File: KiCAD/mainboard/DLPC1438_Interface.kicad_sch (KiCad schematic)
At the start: 84 parts, among them IC3 SN74AUP1G06DCKR, IC4 SN74AUP1G06DCKR, IC5 SN74AUP1G06DCKR, IC6 SN74AUP1G06DCKR, IC7 SN74AUP1G06DCKR, IC8 SN74AUP1G06DCKR, J2 Conn_01x07_Pin, J3 Conn_02x05_Odd_Even, J31 Conn_01x08_Pin, J4 Conn_01x05_Pin, J7 Conn_01x05_Pin, U1 TXS0102DCU, U12 ECS-2520MV-xxx-xx, U13 MX25L3233FM2, U14 SN74AUP1G06DCKR, U22 TXS0102DCU, U5 SN74AUP1G06DCKR

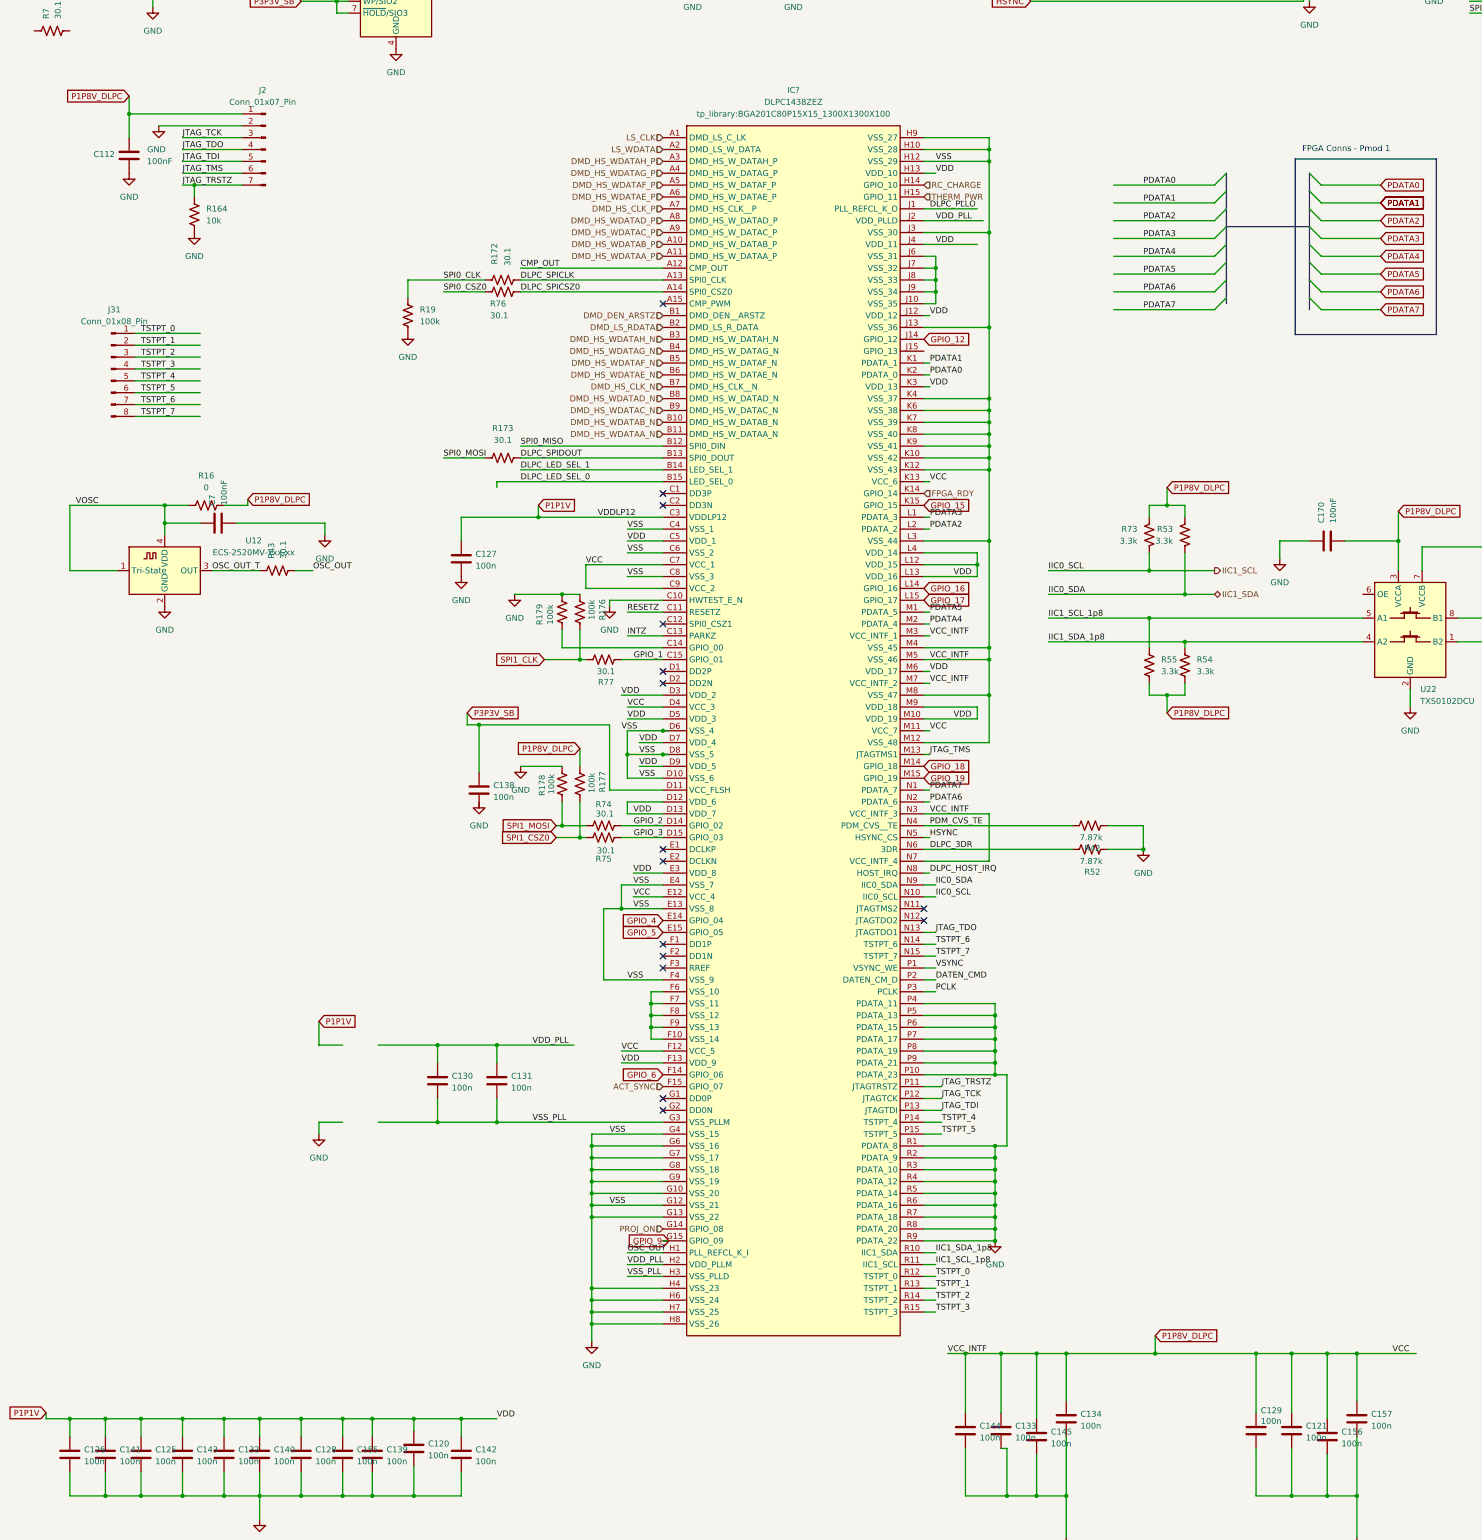
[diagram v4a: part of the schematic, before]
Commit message: fixed bus connection on fpga connector
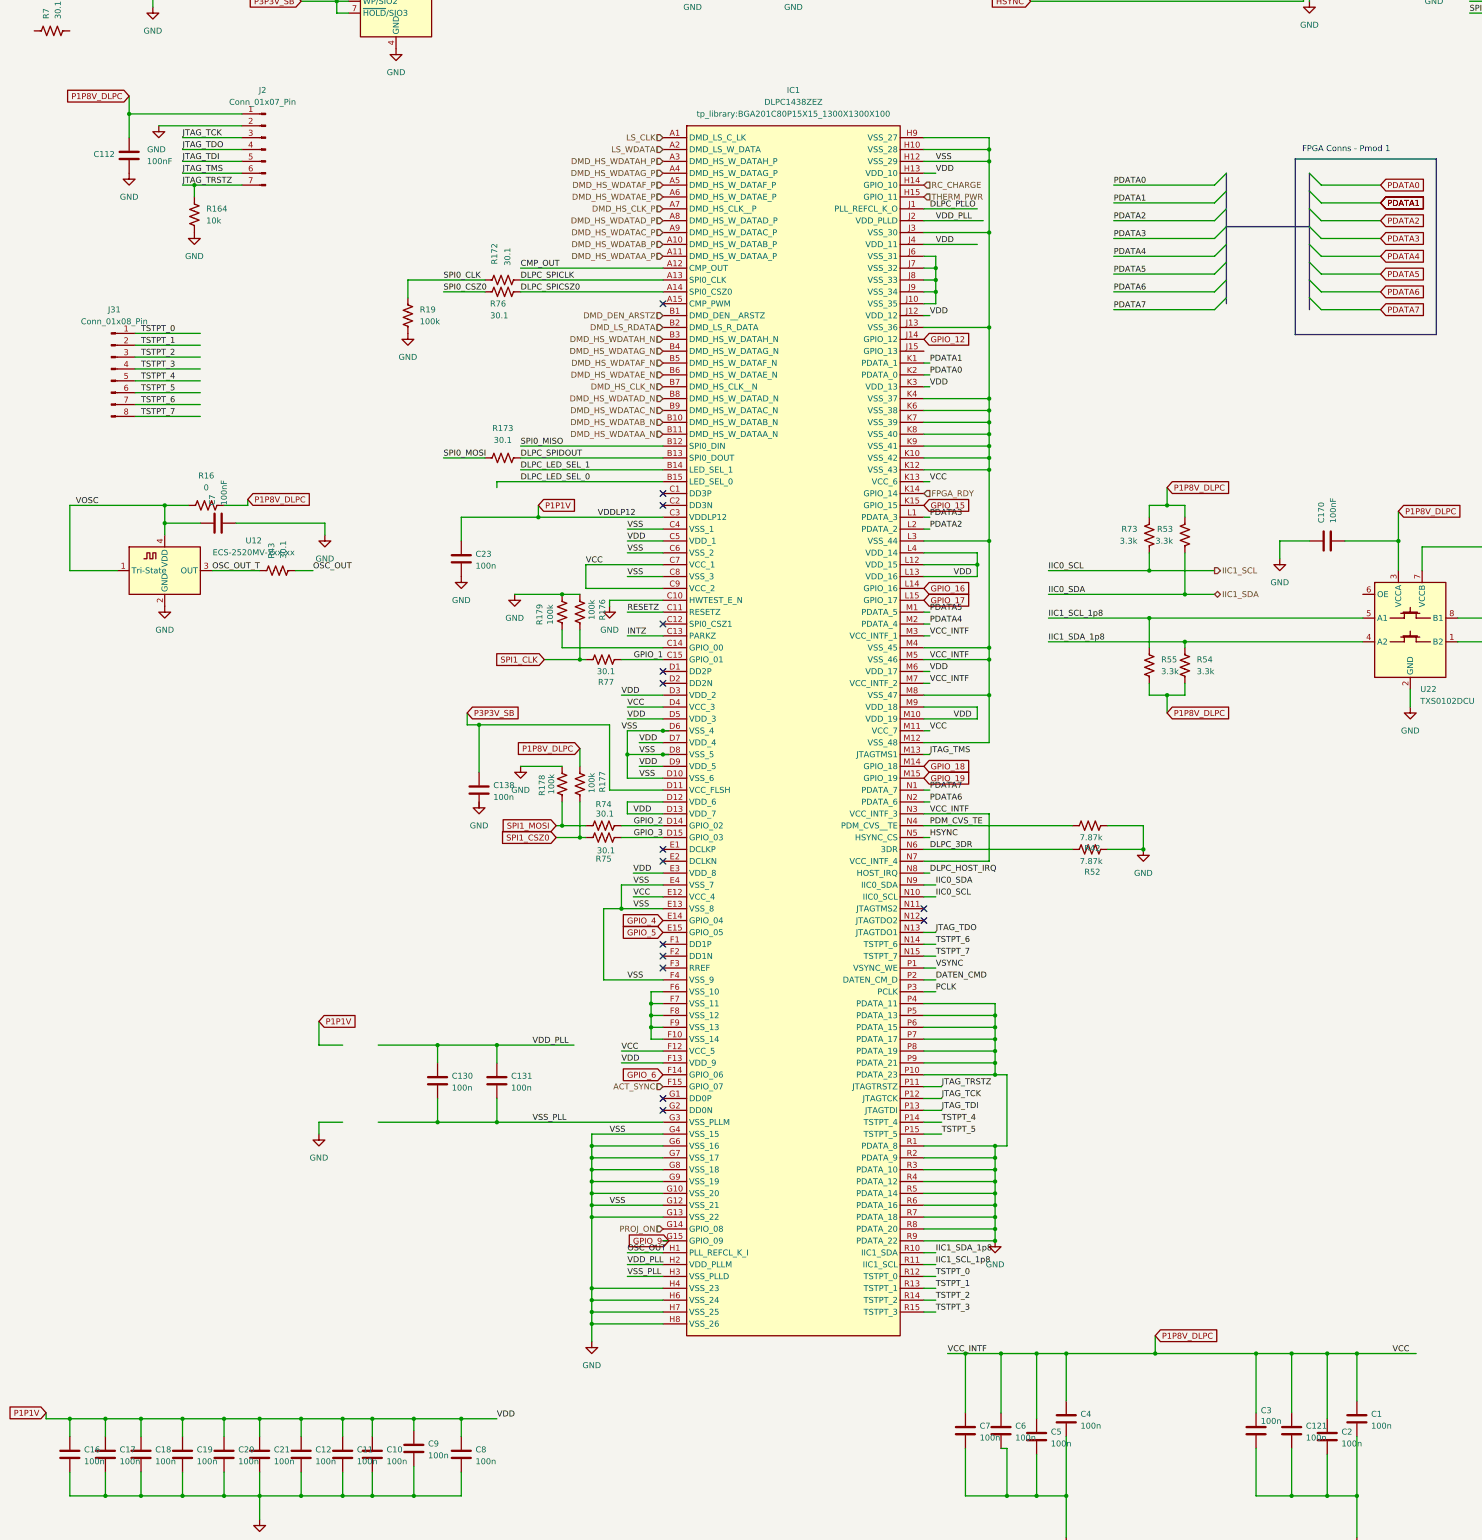
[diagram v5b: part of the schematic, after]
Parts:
- gave numbers to parts that had none: 1
- renumbered C157 to C1, C139 to C10, C155 to C11, C128 to C12, C126 to C16, C141 to C17, C125 to C18, C143 to C19, C156 to C2, C132 to C20, C140 to C21, C127 to C23, C129 to C3, C134 to C4, C145 to C5, C133 to C6, C144 to C7, C142 to C8, C120 to C9

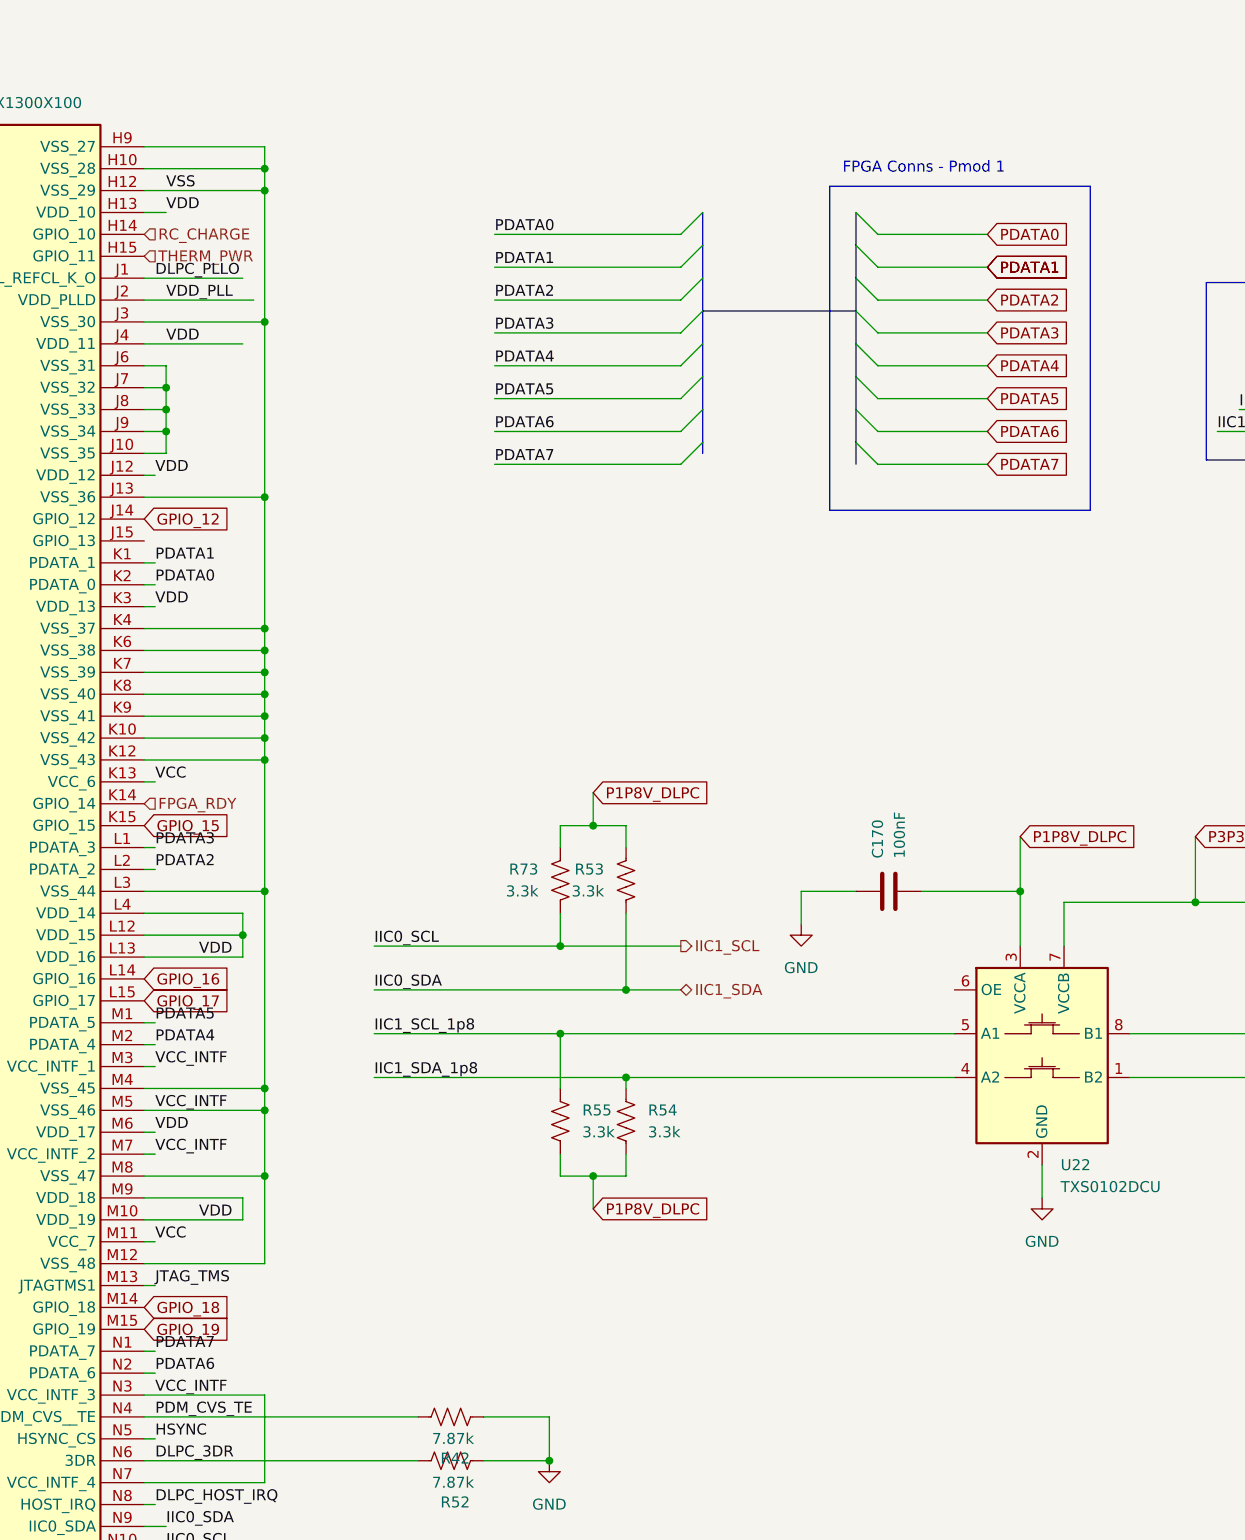
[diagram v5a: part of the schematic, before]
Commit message: fixed pdata bus connection
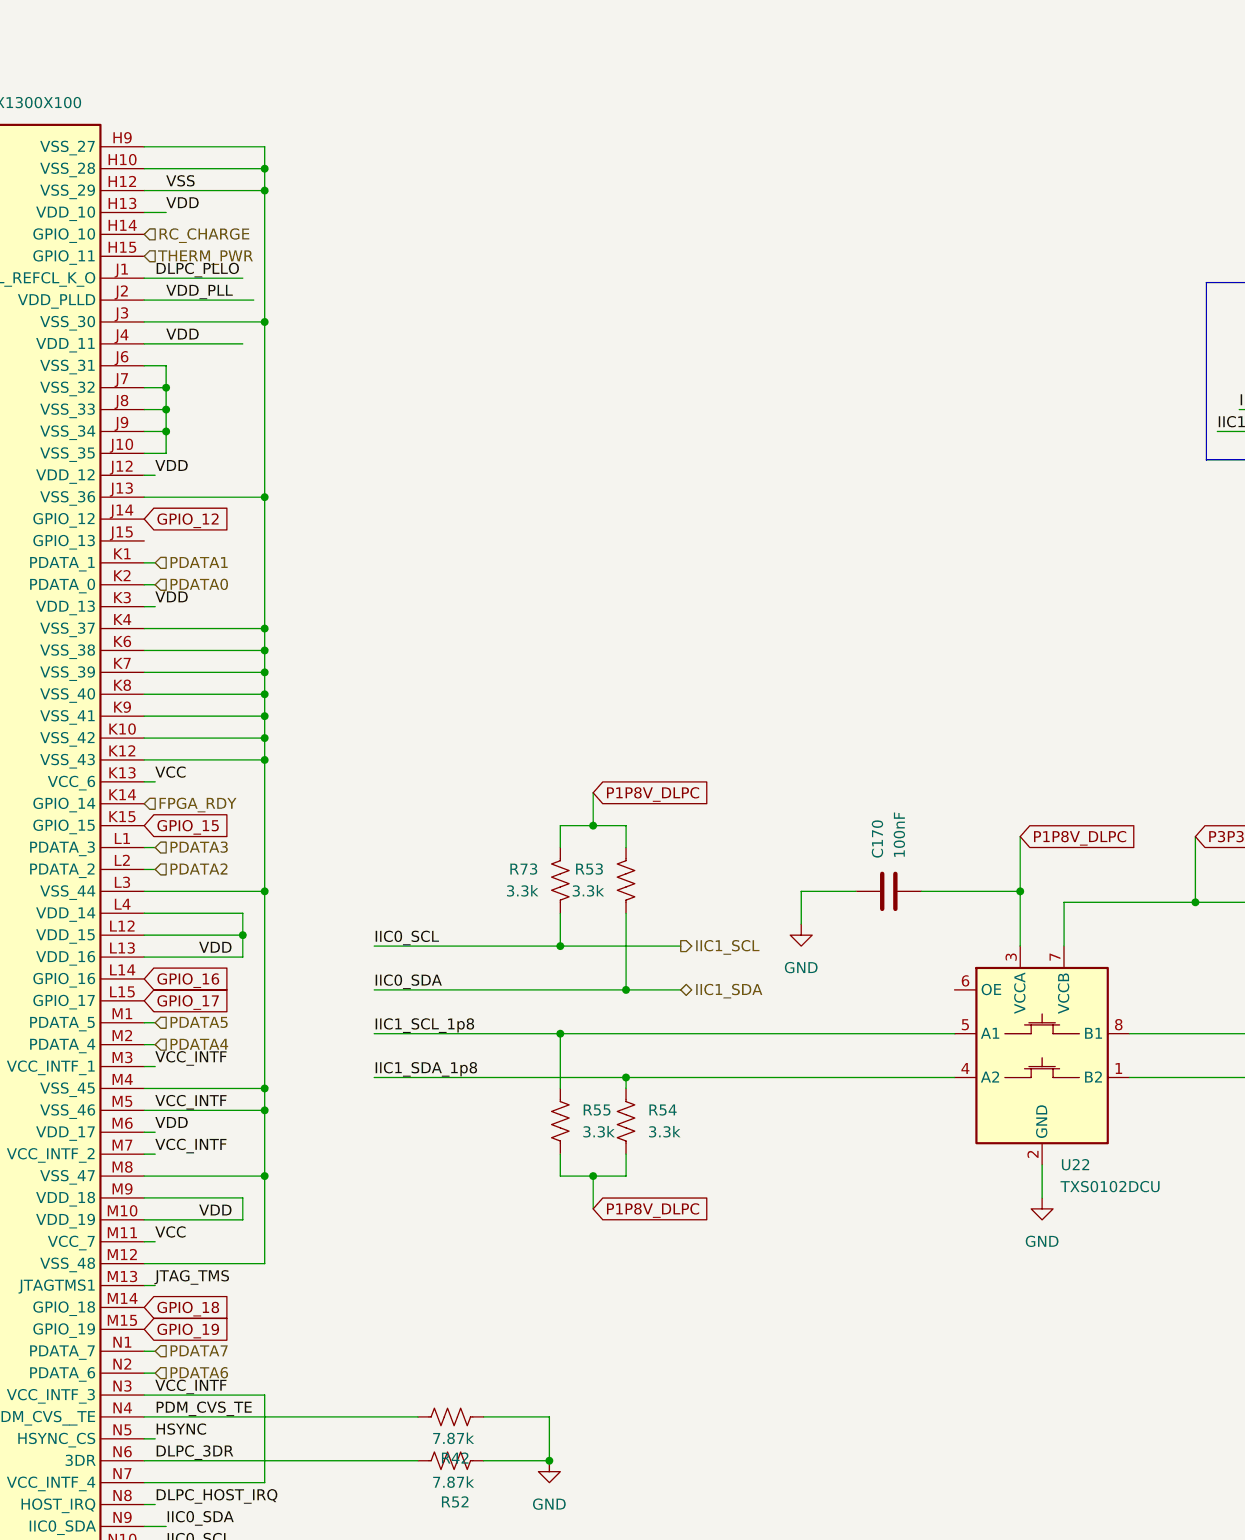
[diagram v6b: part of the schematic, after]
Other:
- note removed: "FPGA Conns - Pmod 1"
